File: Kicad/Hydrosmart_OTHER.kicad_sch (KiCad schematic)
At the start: 6 parts, among them IC1 24FC04HT-I/OT, J2 DNP, U3 CT8122AM-IS3, U4 CT8122AM-IS3

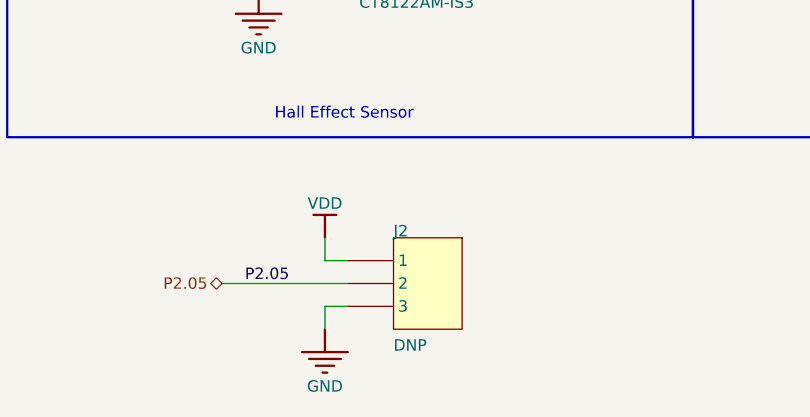
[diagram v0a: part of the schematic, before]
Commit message: + Created library and added information related to BOM: MANUFACTURER and MANUFACTURER PN
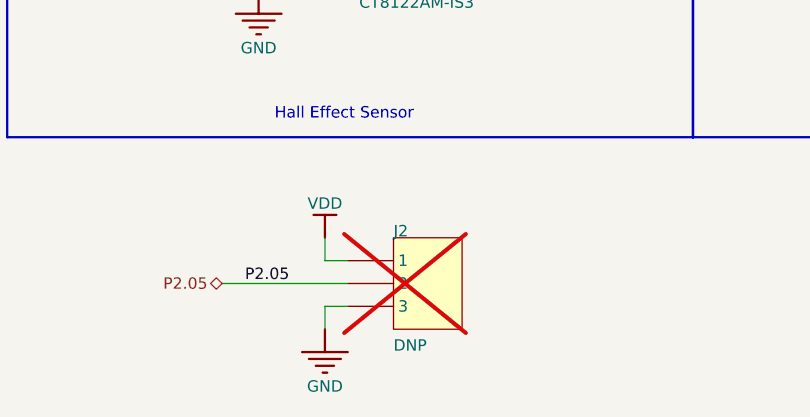
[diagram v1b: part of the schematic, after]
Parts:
- IC1: symbol Hydrosmart_OTHER-altium-import:root_0_24FC04T-I_OT_* -> HydSmart_VA:root_0_24FC04T-I_OT_*; MANUFACTURER (none) -> Microchip; MANUFACTURER_NAME Microchip -> (none); MANUFACTURER_PART_NUMBER 24FC04HT-I/OT -> (none); MANUFACTURER PN (none) -> 24FC04HT-I/OT
- J2: symbol Hydrosmart_OTHER-altium-import:root_0_Header 3_Miscellaneous Connectors.IntLib -> HydSmart_VA:root_0_Header 3_Miscellaneous Connectors.IntLib; now not fitted
- R2, R3: symbol Hydrosmart_OTHER-altium-import:root_1_RES_Altium Content Vault_0 -> HydSmart_VA:root_1_RES_Altium Content Vault_0; MANUFACTURER (none) -> Panasonic Electronic Components; MANUFACTURER_NAME Panasonic Electronic Components -> (none); MANUFACTURER_PART_NUMBER ERJ-2RKF4701X -> (none); MANUFACTURER PN (none) -> ERJ-2RKF4701X
- U3, U4: symbol Hydrosmart_OTHER-altium-import:root_0_CT8122AM-IS3-Symbol-1_Ubihere -> HydSmart_VA:root_0_CT8122AM-IS3-Symbol-1_Ubihere; MANUFACTURER (none) -> Allegro MicroSystems; MANUFACTURER_NAME Allegro MicroSystems -> (none); MANUFACTURER_PART_NUMBER CT8122AM-IS3 -> (none); MANUFACTURER PN (none) -> CT8122AM-IS3
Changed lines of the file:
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@@
 	)
 	(symbol
-		(lib_id "Hydrosmart_OTHER-altium-import:root_1_RES_Altium Content Vault_0")
+		(lib_id "HydSmart_VA:root_1_RES_Altium Content Vault_0")
 		(at 157.48 74.93 0)
 		(unit 1)
@@
 			)
 		)
-		(property "Description" "RES SMD 4.7K OHM 1% 1/10W 0402"
+		(property "Description" "RES SMD 20K OHM 1% 1/10W 0402"
 			(at 157.48 74.93 0)
 			(effects
@@
 			)
 		)
-		(property "MANUFACTURER_NAME" "Panasonic Electronic Components"
-			(at 159.258 66.802 0)
-			(effects
-				(font
-					(size 1.27 1.27)
-				)
-				(justify left bottom)
-				(hide yes)
-			)
-		)
-		(property "MANUFACTURER_PART_NUMBER" "ERJ-2RKF4701X"
-			(at 159.258 66.802 0)
-			(effects
-				(font
-					(size 1.27 1.27)
-				)
-				(justify left bottom)
+		(property "MANUFACTURER" "Panasonic Electronic Components"
+			(at 157.48 74.93 0)
+			(effects
+				(font
+					(size 1.27 1.27)
+				)
+				(hide yes)
+			)
+		)
+		(property "MANUFACTURER PN" "ERJ-2RKF4701X"
+			(at 157.48 74.93 0)
+			(effects
+				(font
+					(size 1.27 1.27)
+				)
 				(hide yes)
 			)
@@
 	)
 	(symbol
-		(lib_id "Hydrosmart_OTHER-altium-import:root_1_RES_Altium Content Vault_0")
+		(lib_id "HydSmart_VA:root_1_RES_Altium Content Vault_0")
 		(at 164.592 74.93 0)
 		(unit 1)
@@
 			)
 		)
-		(property "Description" "RES SMD 4.7K OHM 1% 1/10W 0402"
+		(property "Description" "RES SMD 20K OHM 1% 1/10W 0402"
 			(at 164.592 74.93 0)
 			(effects
@@
 			)
 		)
-		(property "MANUFACTURER_NAME" "Panasonic Electronic Components"
-			(at 166.37 66.802 0)
-			(effects
-				(font
-					(size 1.27 1.27)
-				)
-				(justify left bottom)
-				(hide yes)
-			)
-		)
-		(property "MANUFACTURER_PART_NUMBER" "ERJ-2RKF4701X"
-			(at 166.37 66.802 0)
-			(effects
-				(font
-					(size 1.27 1.27)
-				)
-				(justify left bottom)
+		(property "MANUFACTURER" "Panasonic Electronic Components"
+			(at 164.592 74.93 0)
+			(effects
+				(font
+					(size 1.27 1.27)
+				)
+				(hide yes)
+			)
+		)
+		(property "MANUFACTURER PN" "ERJ-2RKF4701X"
+			(at 164.592 74.93 0)
+			(effects
+				(font
+					(size 1.27 1.27)
+				)
 				(hide yes)
 			)
@@
 	)
 	(symbol
-		(lib_id "Hydrosmart_OTHER-altium-import:root_0_24FC04T-I_OT_*")
+		(lib_id "HydSmart_VA:root_0_24FC04T-I_OT_*")
 		(at 168.91 81.28 0)
 		(unit 1)
@@
 			)
 		)
-		(property "MANUFACTURER_NAME" "Microchip"
-			(at 168.402 78.74 0)
-			(effects
-				(font
-					(size 1.27 1.27)
-				)
-				(justify left bottom)
-				(hide yes)
-			)
-		)
-		(property "MANUFACTURER_PART_NUMBER" "24FC04HT-I/OT"
-			(at 168.402 78.74 0)
-			(effects
-				(font
-					(size 1.27 1.27)
-				)
-				(justify left bottom)
-				(hide yes)
-			)
-		)
 		(property "DIGIKEY PART NUMBER" "24FC04HT-I/OTCT-ND"
 			(at 168.402 78.74 0)
@@
 			)
 		)
+		(property "MANUFACTURER" "Microchip"
+			(at 168.91 81.28 0)
+			(effects
+				(font
+					(size 1.27 1.27)
+				)
+				(hide yes)
+			)
+		)
+		(property "MANUFACTURER PN" "24FC04HT-I/OT"
+			(at 168.91 81.28 0)
+			(effects
+				(font
+					(size 1.27 1.27)
+				)
+				(hide yes)
+			)
+		)
 		(pin "4"
 		)
@@
 	)
 	(symbol
-		(lib_id "Hydrosmart_OTHER-altium-import:root_0_CT8122AM-IS3-Symbol-1_Ubihere")
+		(lib_id "HydSmart_VA:root_0_CT8122AM-IS3-Symbol-1_Ubihere")
 		(at 93.98 101.6 0)
 		(unit 1)
@@
 			)
 		)
-		(property "MANUFACTURER_NAME" "Allegro MicroSystems"
-			(at 93.472 96.52 0)
-			(effects
-				(font
-					(size 1.27 1.27)
-				)
-				(justify left bottom)
-				(hide yes)
-			)
-		)
-		(property "MANUFACTURER_PART_NUMBER" "CT8122AM-IS3"
-			(at 93.472 96.52 0)
-			(effects
-				(font
-					(size 1.27 1.27)
-				)
-				(justify left bottom)
+		(property "MANUFACTURER" "Allegro MicroSystems"
+			(at 93.98 101.6 0)
+			(effects
+				(font
+					(size 1.27 1.27)
+				)
+				(hide yes)
+			)
+		)
+		(property "MANUFACTURER PN" "CT8122AM-IS3"
+			(at 93.98 101.6 0)
+			(effects
+				(font
+					(size 1.27 1.27)
+				)
 				(hide yes)
 			)
@@
 	)
 	(symbol
-		(lib_id "Hydrosmart_OTHER-altium-import:root_0_CT8122AM-IS3-Symbol-1_Ubihere")
+		(lib_id "HydSmart_VA:root_0_CT8122AM-IS3-Symbol-1_Ubihere")
 		(at 93.98 73.66 0)
 		(unit 1)
@@
 			)
 		)
-		(property "MANUFACTURER_NAME" "Allegro MicroSystems"
-			(at 93.472 68.58 0)
-			(effects
-				(font
-					(size 1.27 1.27)
-				)
-				(justify left bottom)
-				(hide yes)
-			)
-		)
-		(property "MANUFACTURER_PART_NUMBER" "CT8122AM-IS3"
-			(at 93.472 68.58 0)
-			(effects
-				(font
-					(size 1.27 1.27)
-				)
-				(justify left bottom)
+		(property "MANUFACTURER" "Allegro MicroSystems"
+			(at 93.98 73.66 0)
+			(effects
+				(font
+					(size 1.27 1.27)
+				)
+				(hide yes)
+			)
+		)
+		(property "MANUFACTURER PN" "CT8122AM-IS3"
+			(at 93.98 73.66 0)
+			(effects
+				(font
+					(size 1.27 1.27)
+				)
 				(hide yes)
 			)
@@
 	)
 	(symbol
-		(lib_id "Hydrosmart_OTHER-altium-import:root_0_Header 3_Miscellaneous Connectors.IntLib")
+		(lib_id "HydSmart_VA:root_0_Header 3_Miscellaneous Connectors.IntLib")
 		(at 105.41 137.16 0)
 		(unit 1)
@@
 		(in_bom yes)
 		(on_board yes)
-		(dnp no)
+		(dnp yes)
 		(property "Reference" "J2"
 			(at 105.41 137.16 0)
